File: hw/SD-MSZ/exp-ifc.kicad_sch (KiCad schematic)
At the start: 66 parts, among them J10 Conn_02x02 HDR, J11 Conn_02x03, J12 CONN 02x05 - DTE_HDR-AES, J13 HDR 2x4, J15 Screw_Terminal_01x02, J16 Conn_01x08 SCKT, J17 Conn_02x10 HDR, J18 Conn_02x10 HDR, J19 Conn_02x17 (34P Ribbon), J20 1x40 90° PIN STRIP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

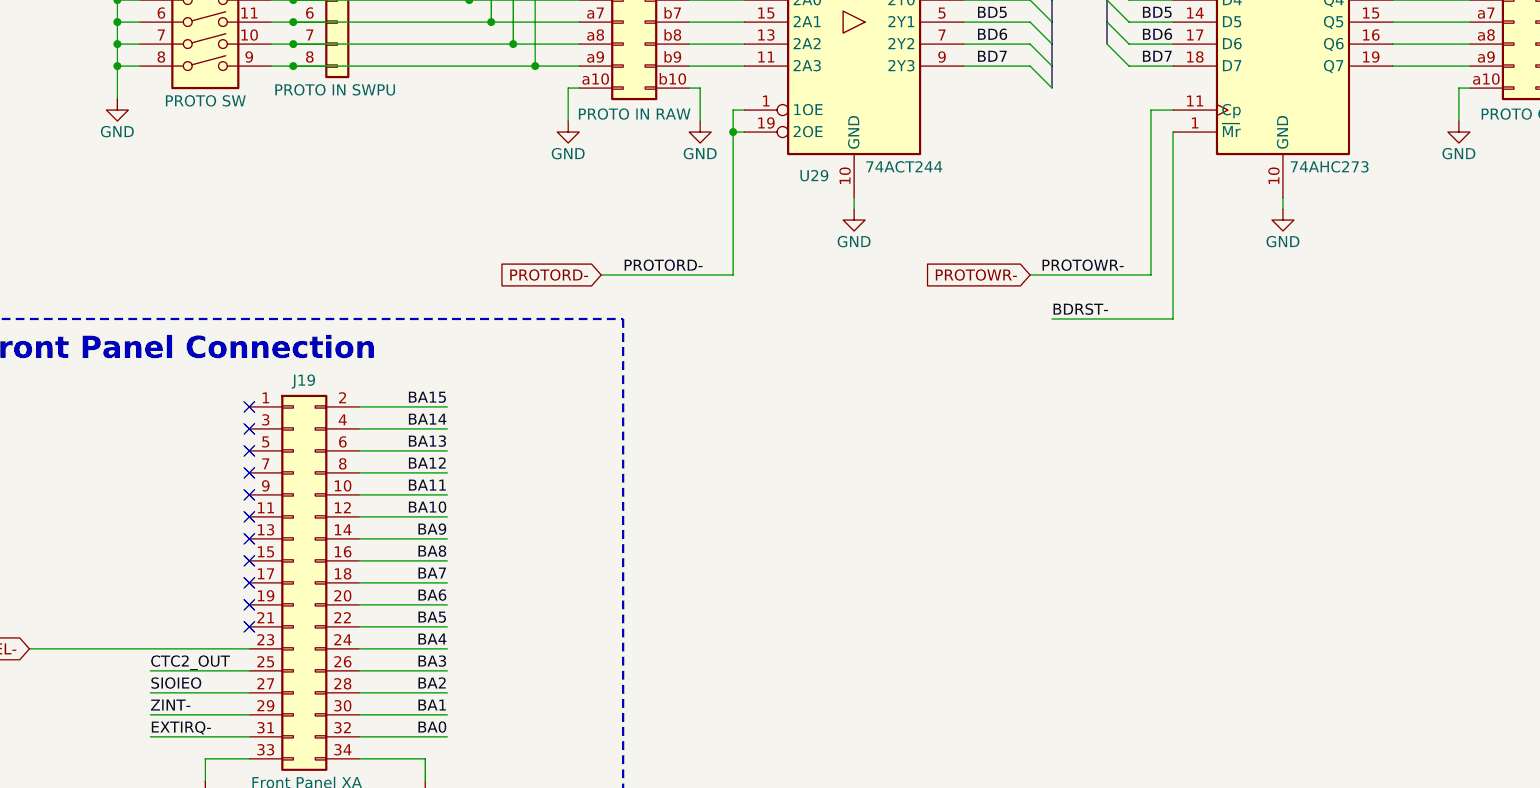
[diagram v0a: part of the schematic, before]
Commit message: Update gitignore to skip KiCad lock and backup files.
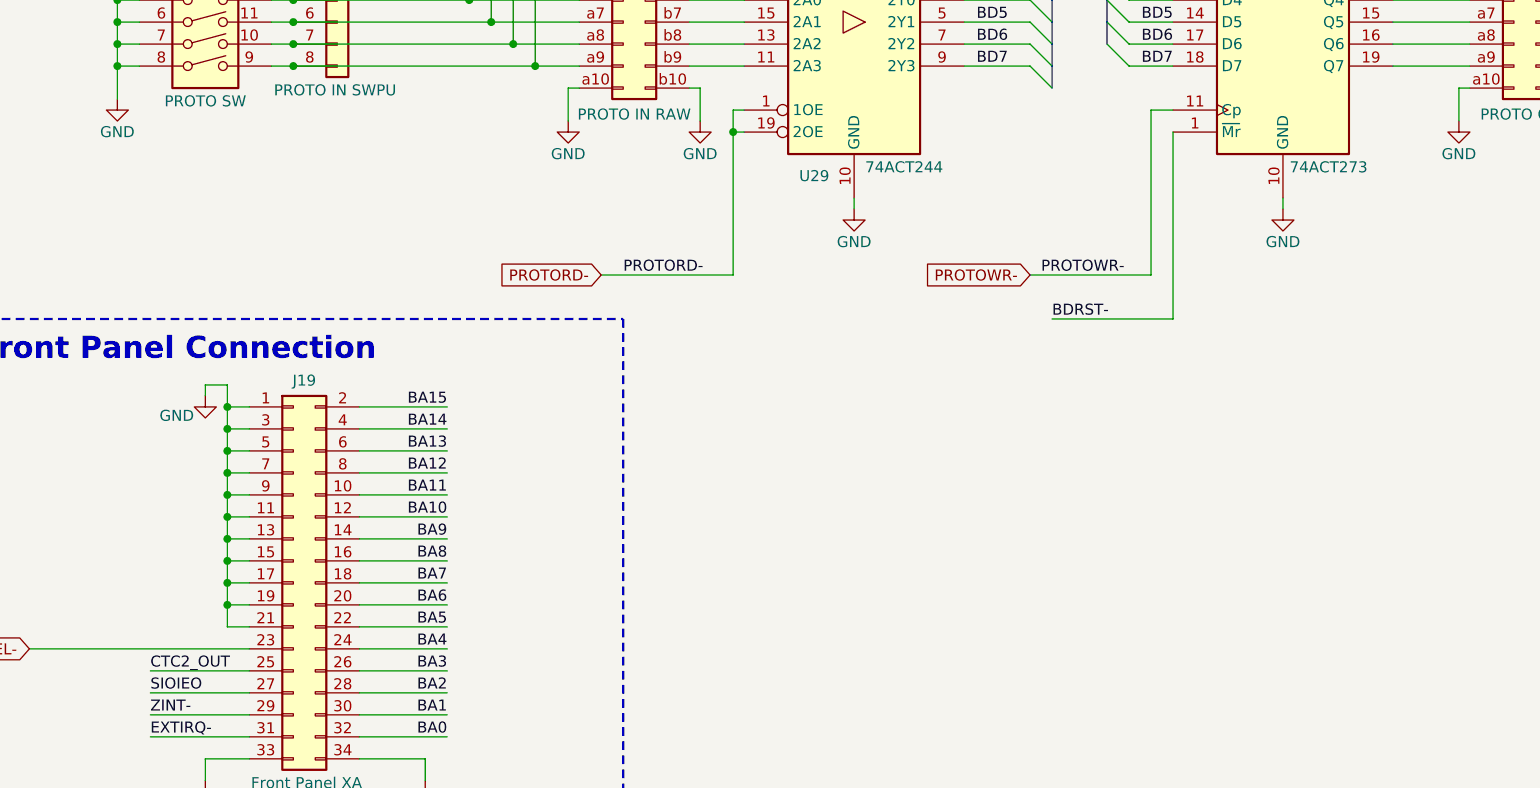
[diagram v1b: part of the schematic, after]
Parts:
- U30: value 74AHC273 -> 74ACT273
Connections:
- net GND: now also J19.1 (Pin_1), J19.11 (Pin_11), J19.13 (Pin_13), J19.15 (Pin_15), J19.17 (Pin_17), J19.19 (Pin_19), J19.21 (Pin_21), J19.3 (Pin_3), J19.5 (Pin_5), J19.7 (Pin_7), J19.9 (Pin_9)
- no-connect marks 28 -> 17
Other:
- company: Silky Design -> SilkyDESIGN
- title: SIO, CTC, and ExpIFC -> CTC, SIO, Front Pnl Conn, RC2014 Bus
